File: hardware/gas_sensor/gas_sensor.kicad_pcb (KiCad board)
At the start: 2 copper layers, 45.5 x 32.5 mm, 15 parts, among them J1 Conn_01x04, U1 LM393

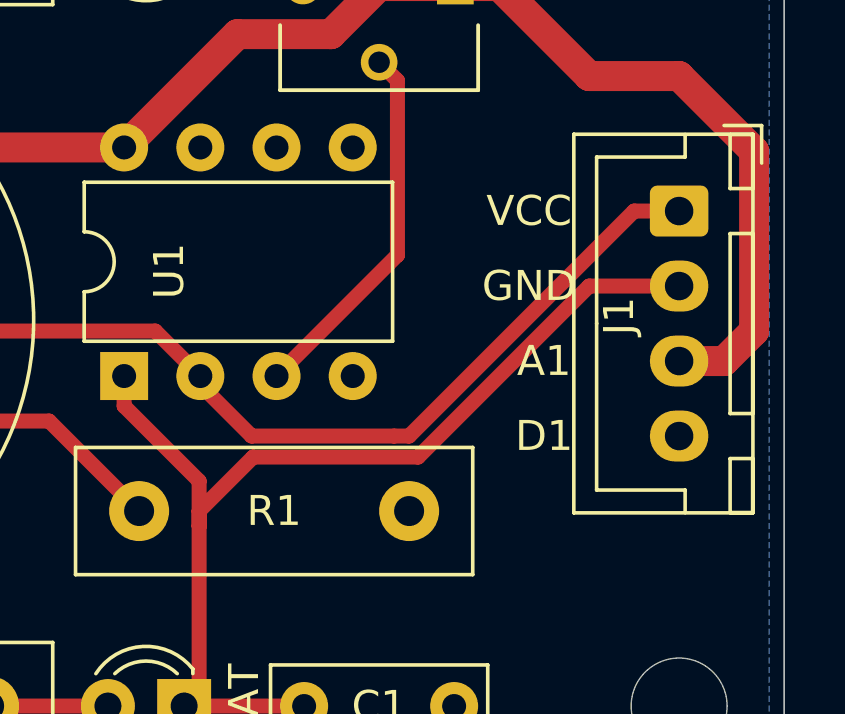
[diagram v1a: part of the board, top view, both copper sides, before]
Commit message: Update temp and gas sensors
Minor changes: added screenshots of temp/humidity sensor, changed gas sensor pin names on PCB
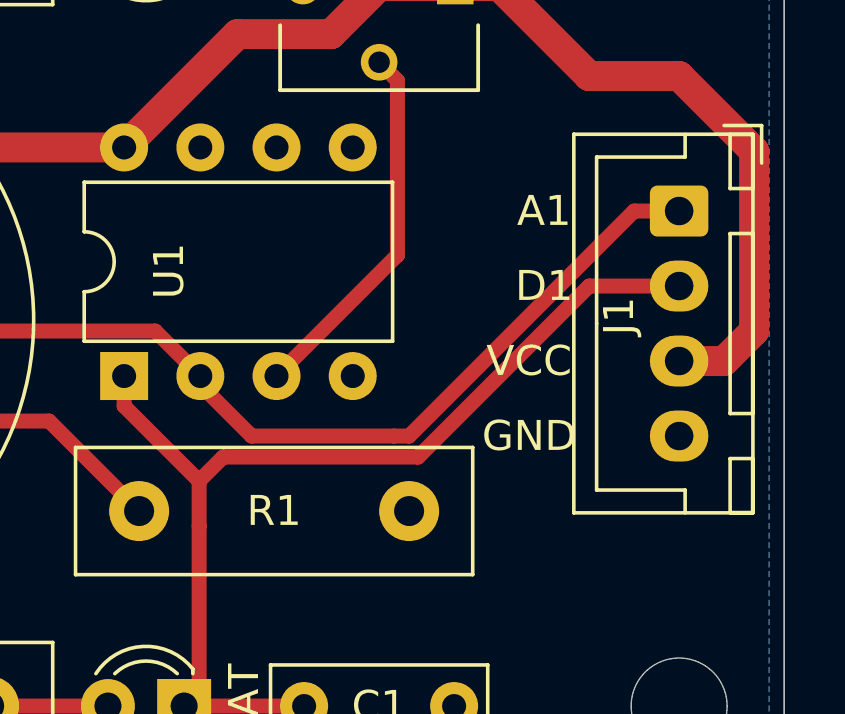
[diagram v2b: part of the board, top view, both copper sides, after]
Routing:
- net D1: track 35.8 -> 34.9 mm

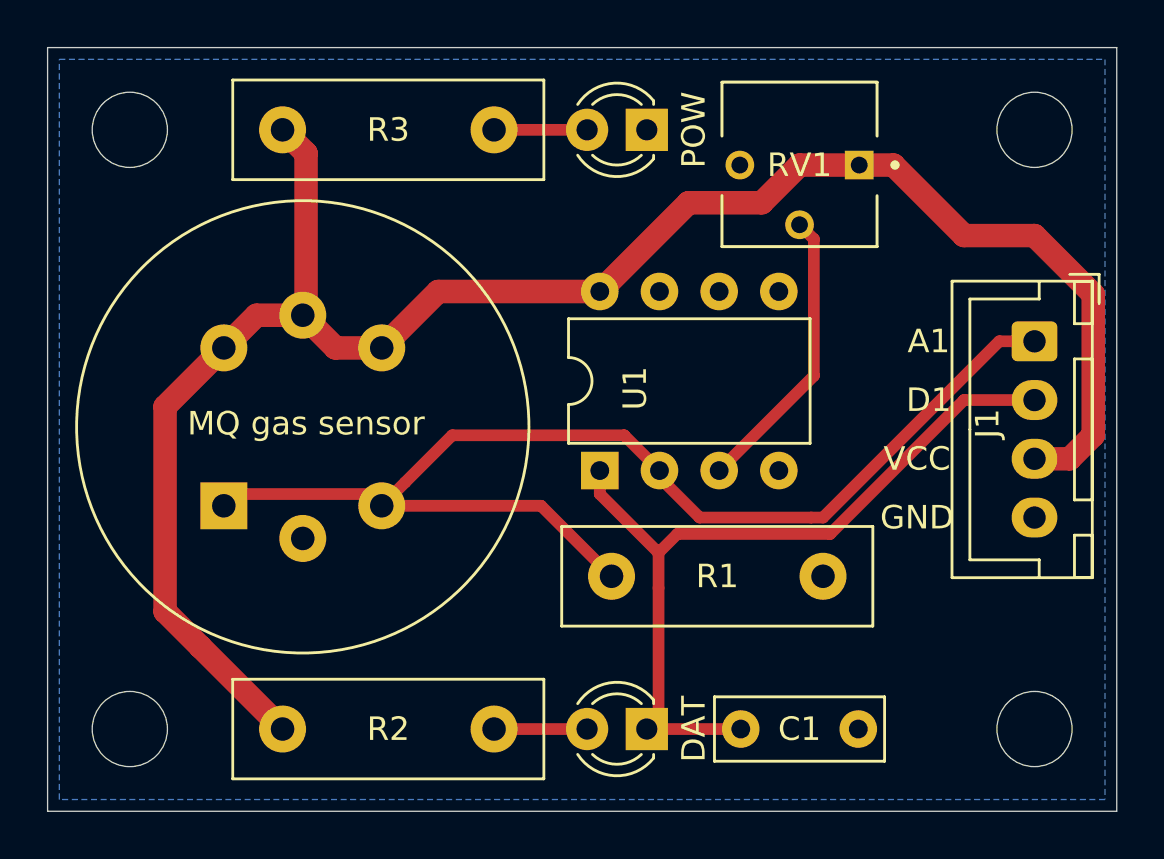
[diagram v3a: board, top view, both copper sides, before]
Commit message: Update on 12V5A system power line
- 12V5A power line is now represented by two connectors with 2 pins across all the modules
- all .png previews are updated. The central hub now has previews for schematics, PCB tracing and 3D model
- peltier module now has two 12V5A connectors with redesigned one side of the bridge. Now all MOSFETs can be equipped with heatsinks
- hum/temp sensor now has its connector position reversed to mimic Grove's one
- hum/temp and gas sensors now have a small BeeHive logo on front layer rather than one big on back layer
- hum/temp sensor now use only one layer for signals and one layer for ground
- switch arrays now have two connectors for 12V5A and 5V3A power lines
- switch arrays had their power lines better traced (no sharp turns)
- power supply (12V5A to 5V3A) now has two connectors for 12V5A power line
- one trace of power supply, which lies in between LM2596's legs, was narrowed to ensure that it will not be accidentally soldered or damaged during placement
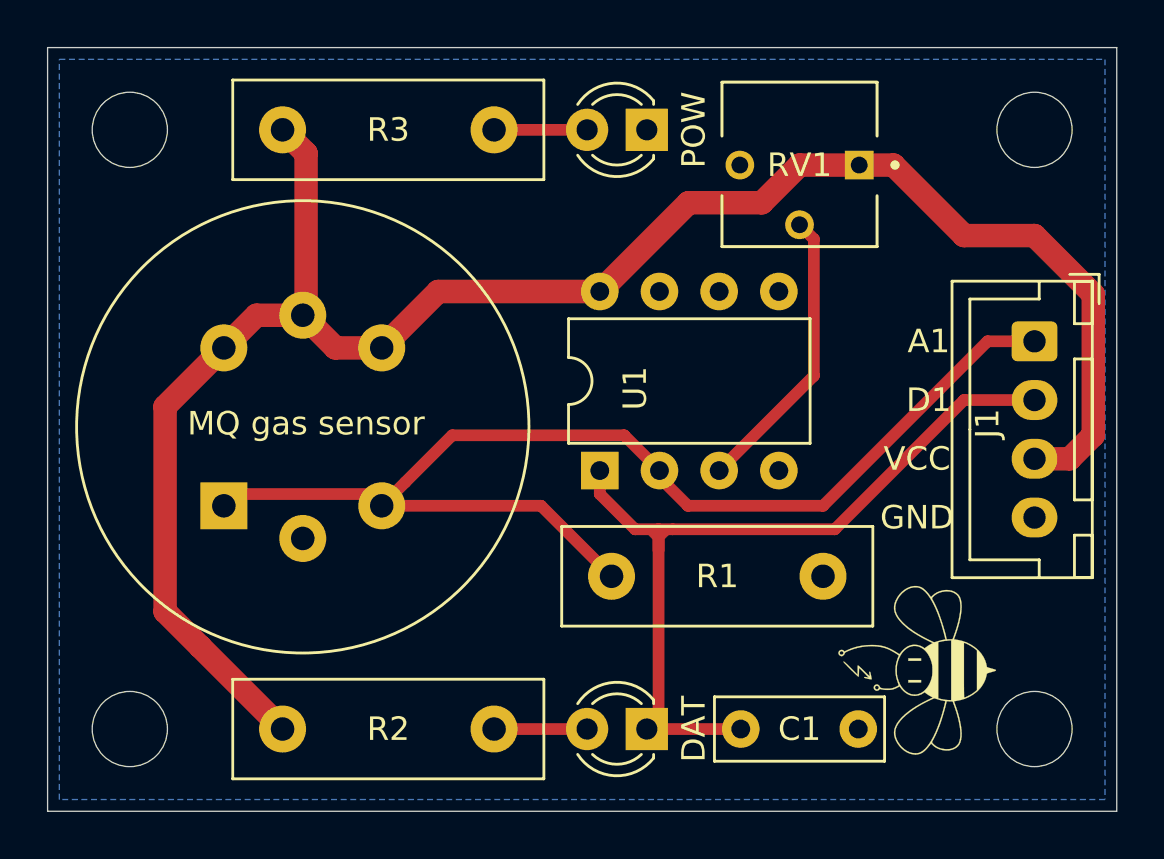
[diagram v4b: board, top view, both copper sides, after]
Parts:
- removed the G*** at (159.0, 103.0)
- added G***: LOGO, logo-beehive:logo-beehive-7_2х6_7mm, F.Cu at (161.0, 113.5)
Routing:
- net D1: track 34.9 -> 37.4 mm
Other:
- rule pad_to_mask_clearance: 0.051 -> 0

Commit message: Add version number to boards
Add version number to boards and update screenshots, zip gerber archives
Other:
- board text added: "MQ gas sensor v0.1"
- board text removed: "MQ gas sensor"

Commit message: Apply CERN-W license
Apply CERN-W license to all boards, move the first iteration of the IR_sensor to the archive

Co-Authored-By: Andre Maia Chagas <a.maia-chagas@sussex.ac.uk>
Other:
- board text added: "board by Ihor Sobianin licensed under CERN-OHL-W 2.0 https://ohwr.org/project/cernohl"

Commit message: boards review
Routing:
- net +5V: track 80.3 -> 81.5 mm
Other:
- board text added: "MQ gas sensor v0.2"
- board text removed: "MQ gas sensor v0.1"
